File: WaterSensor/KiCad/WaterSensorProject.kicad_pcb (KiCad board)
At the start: 2 copper layers, 17 parts, among them Q1_A1 TEPT4400, Q1_B1 TEPT4400, U1 TLV7042DDFR, U2 ESP32-C3, U3 RP604K331A-TR

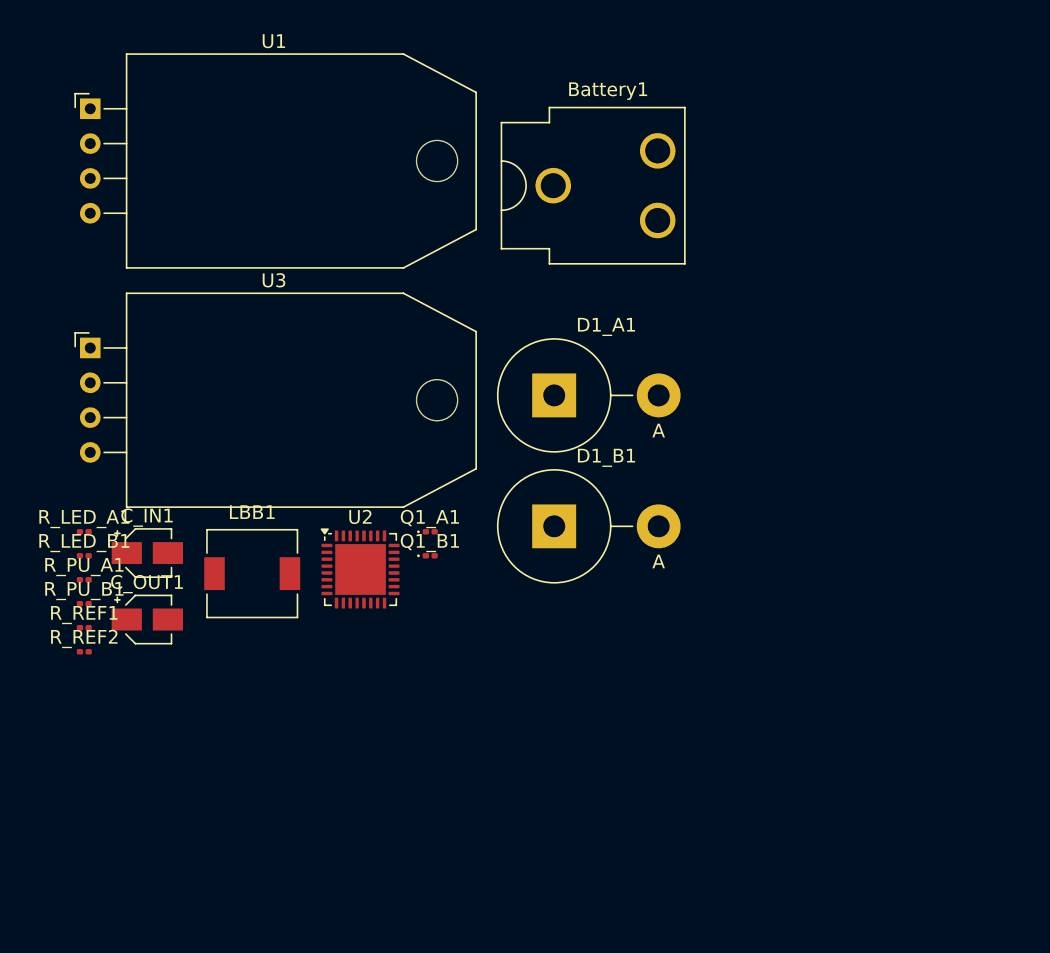
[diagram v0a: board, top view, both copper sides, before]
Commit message: Updated schematic, created 2 pcbs with tracks, proper footprints & models
- Updated schematic
- Downloaded, imported all correct footprints and models
- Created 2 viable PCBs with tracks
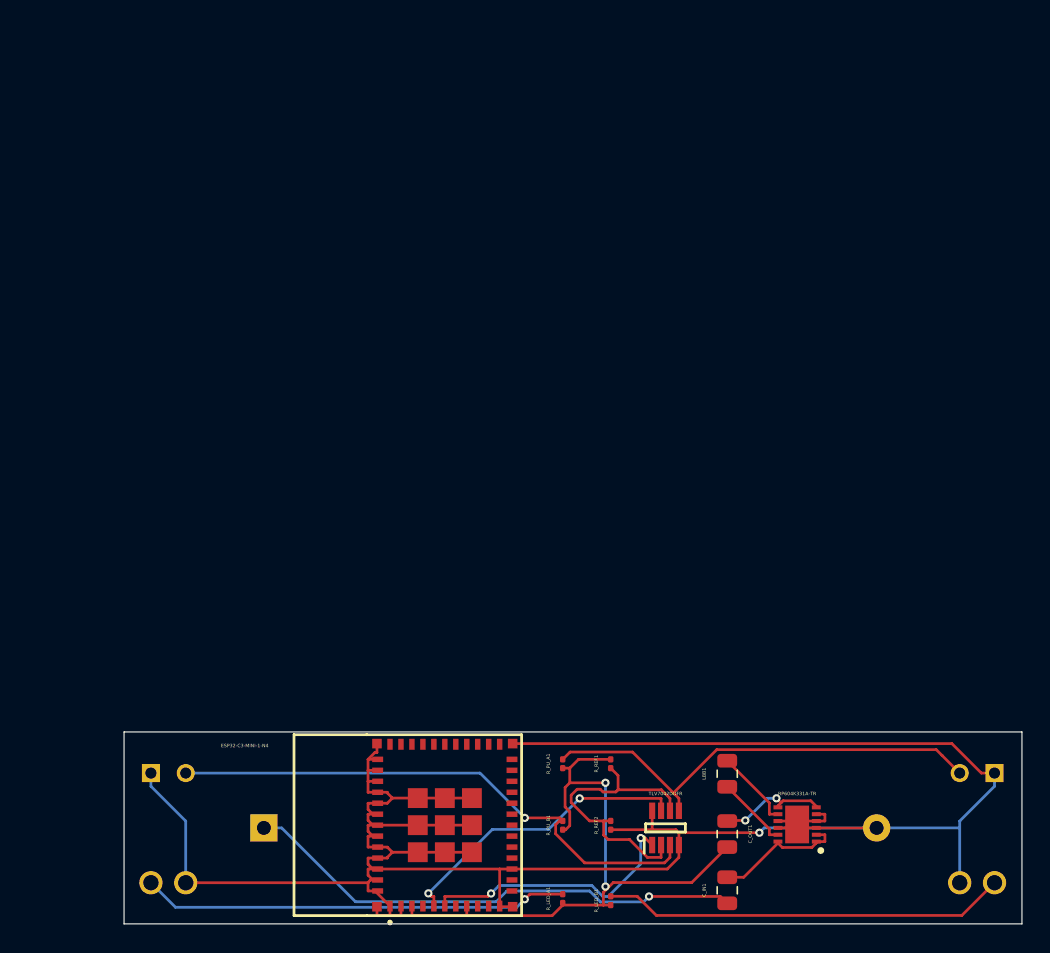
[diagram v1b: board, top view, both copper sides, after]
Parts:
- Battery1: footprint Battery:BatteryClip_Keystone_54_D16-19mm -> Battery:BatteryHolder_Keystone_2466_1xAAA; moved to B.Cu
- C_IN1, C_OUT1: footprint Capacitor_SMD:CP_Elec_3x5.3 -> Capacitor_SMD:C_0805_2012Metric
- D1_A1, D1_B1: footprint Diode_THT:D_5KPW_P7.62mm_Vertical_AnodeUp -> TSAL6200:TSAL6200; moved to B.Cu
- LBB1: footprint Inductor_SMD:L_6.3x6.3_H3 -> Capacitor_SMD:C_0805_2012Metric
- Q1_A1, Q1_B1: footprint Diode_SMD:D_0201_0603Metric -> TEPT4400:LED_TEPT4400_VIS; moved to B.Cu
- U1: value TLV7042DDFR -> RP604K331A-TR; footprint Sensor:ASAIR_AM2302_P2.54mm_Lead2.75mm_TabDown -> RP604K331A-TR:SON50P270X300X60-13N
- U2: value ESP32-C3 -> ESP32-C3-MINI-1-N4; footprint Package_DFN_QFN:QFN-32-1EP_5x5mm_P0.5mm_EP3.7x3.7mm -> ESP32-C3-MINI-1-N4:ESP32C3MINI1N4
- U3: value RP604K331A-TR -> TLV7042DDFR; footprint Sensor:ASAIR_AM2302_P2.54mm_Lead2.75mm_TabDown -> TLV7042DDFR:SOT65P280X110-8N
- moved U1 73.4 mm to (117.6, 93.8), turned to 180 degrees
- moved U3 54.7 mm to (108.0, 94.0), turned to 90 degrees
- moved Battery1 51.4 mm to (78.7, 94.0)
- moved C_IN1 48.9 mm to (112.5, 98.5), turned to 90 degrees
- moved R_LED_B1 45.9 mm to (104.0, 99.3), turned to 90 degrees
- moved D1_A1 45.3 mm to (71.7, 98.0)
- moved C_OUT1 45.1 mm to (112.5, 94.5), turned to -90 degrees
- moved Q1_B1 44.1 mm to (132.0, 90.0), turned to 180 degrees
- moved R_LED_A1 44.0 mm to (100.5, 99.2), turned to 90 degrees
- moved R_REF2 40.4 mm to (104.0, 93.8), turned to 90 degrees
- moved D1_B1 40.3 mm to (130.7, 98.0), turned to 180 degrees
- moved R_REF1 39.7 mm to (104.0, 89.3), turned to 90 degrees
- moved R_PU_B1 38.5 mm to (100.5, 93.8), turned to 90 degrees
- moved LBB1 37.6 mm to (112.5, 90.0), turned to 90 degrees
- moved R_PU_A1 37.4 mm to (100.5, 89.3), turned to 90 degrees
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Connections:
- C_IN1 pad 2: Net-(U3-CE) -> Net-(U1-AVIN)
- C_OUT1 pad 1: Net-(U3-VOUT) -> Net-(U1-VFB)
- C_OUT1 pad 2: Net-(U2-CHIP_EN) -> Net-(U2-3V3)
- D1_A1 pad 1: Net-(Battery1--) -> Net-(D1_A1-A)
- D1_A1 pad 2: Net-(D1_A1-Pad2) -> Net-(Battery1--)
- D1_B1 pad 1: Net-(Battery1--) -> Net-(D1_B1-A)
- D1_B1 pad 2: Net-(D1_B1-Pad2) -> Net-(Battery1--)
- LBB1 pad 1: Net-(U3-BULX) -> Net-(U1-BULX)
- LBB1 pad 2: Net-(U3-BOLX) -> Net-(U1-BOLX)
- Q1_A1 pad 2: Net-(U1-ina+) -> Net-(U3-INA+)
- Q1_B1 pad 2: Net-(U1-inb+) -> Net-(U3-INB+)
- R_LED_A1 pad 1: Net-(U2-CHIP_EN) -> Net-(U2-3V3)
- R_LED_A1 pad 2: Net-(D1_A1-Pad2) -> Net-(D1_A1-A)
- R_LED_B1 pad 1: Net-(U2-CHIP_EN) -> Net-(U2-3V3)
- R_LED_B1 pad 2: Net-(D1_B1-Pad2) -> Net-(D1_B1-A)
- R_PU_A1 pad 1: Net-(U2-CHIP_EN) -> Net-(U2-3V3)
- R_PU_A1 pad 2: Net-(U1-inb+) -> Net-(U3-INB+)
- R_PU_B1 pad 1: Net-(U2-CHIP_EN) -> Net-(U2-3V3)
- R_PU_B1 pad 2: Net-(U1-ina+) -> Net-(U3-INA+)
- R_REF1 pad 1: Net-(U1-ina-) -> Net-(U3-INA-)
- R_REF1 pad 2: Net-(U2-CHIP_EN) -> Net-(U2-3V3)
- R_REF2 pad 2: Net-(U1-ina-) -> Net-(U3-INA-)
- U1 pad 1: Net-(U1-outa) -> Net-(U1-AVIN)
- U1 pad 2: Net-(U1-ina-) -> Net-(U1-AVIN)
- U1 pad 3: Net-(U1-ina+) -> Net-(Battery1--)
- U2 pad 1: unconnected-(U2-LNA_IN-Pad1) -> Net-(Battery1--)
- U2 pad 11: unconnected-(U2-VDD3P3_RTC-Pad11) -> Net-(Battery1--)
- U2 pad 14: unconnected-(U2-GPIO8-Pad14) -> Net-(Battery1--)
- U2 pad 2: Net-(U2-CHIP_EN) -> Net-(Battery1--)
- U2 pad 3: Net-(U2-CHIP_EN) -> Net-(U2-3V3)
- U2 pad 31: Net-(U2-VDDA-Pad31) -> unconnected-(U2-TXD0-Pad31)
- U2 pad 32: Net-(U2-VDDA-Pad31) -> unconnected-(U2-NC_11-Pad32)
- U2 pad 33: Net-(Battery1--) -> unconnected-(U2-NC_12-Pad33)
- U2 pad 5: unconnected-(U2-XTAL_32K_N-Pad5) -> Net-(U2-IO2)
- U2 pad 6: Net-(U1-outa) -> Net-(U2-IO3)
- U2 pad 7: Net-(U2-CHIP_EN) -> unconnected-(U2-NC_2-Pad7)
- U2 pad 8: Net-(U1-outb) -> Net-(U2-3V3)
- U3 pad 1: unconnected-(U3-AVIN-Pad1) -> Net-(U2-IO3)
- U3 pad 2: Net-(U3-CE) -> Net-(U3-INA-)
- U3 pad 3: unconnected-(U3-PGND-Pad3) -> Net-(U3-INA+)
- U3 pad 4: unconnected-(U3-PGND-Pad4) -> Net-(Battery1--)
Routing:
- net Net-(Battery1--): track 0.00 -> 182.7 mm, vias 0 -> 1
- net Net-(U2-3V3): track 0.00 -> 47.0 mm, vias 0 -> 2
- net Net-(U3-INA+): track 0.00 -> 40.5 mm, vias 0 -> 1
- net Net-(Battery1-+): track 0.00 -> 37.1 mm, vias 0 -> 1
- net Net-(U3-INB+): track 0.00 -> 33.9 mm
- net Net-(D1_A1-A): track 0.00 -> 31.2 mm, vias 0 -> 1
- net Net-(D1_B1-A): track 0.00 -> 29.6 mm
- net Net-(U2-IO2): track 0.00 -> 21.9 mm, vias 0 -> 2
- net Net-(U3-INA-): track 0.00 -> 21.3 mm
- net Net-(U2-IO3): track 0.00 -> 19.6 mm, vias 0 -> 2
- net Net-(U1-AVIN): track 0.00 -> 9.76 mm
- net Net-(U1-VFB): track 0.00 -> 8.05 mm, vias 0 -> 2
- net Net-(U1-BOLX): track 0.00 -> 5.80 mm
- net Net-(U1-BULX): track 0.00 -> 5.40 mm
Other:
- board outline added: 65.5 x 14 mm
